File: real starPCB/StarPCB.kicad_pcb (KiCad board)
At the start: 2 copper layers, 19.6 x 19.2 mm, 5 parts, among them J1 +, J2 +, J4 -, J5 -

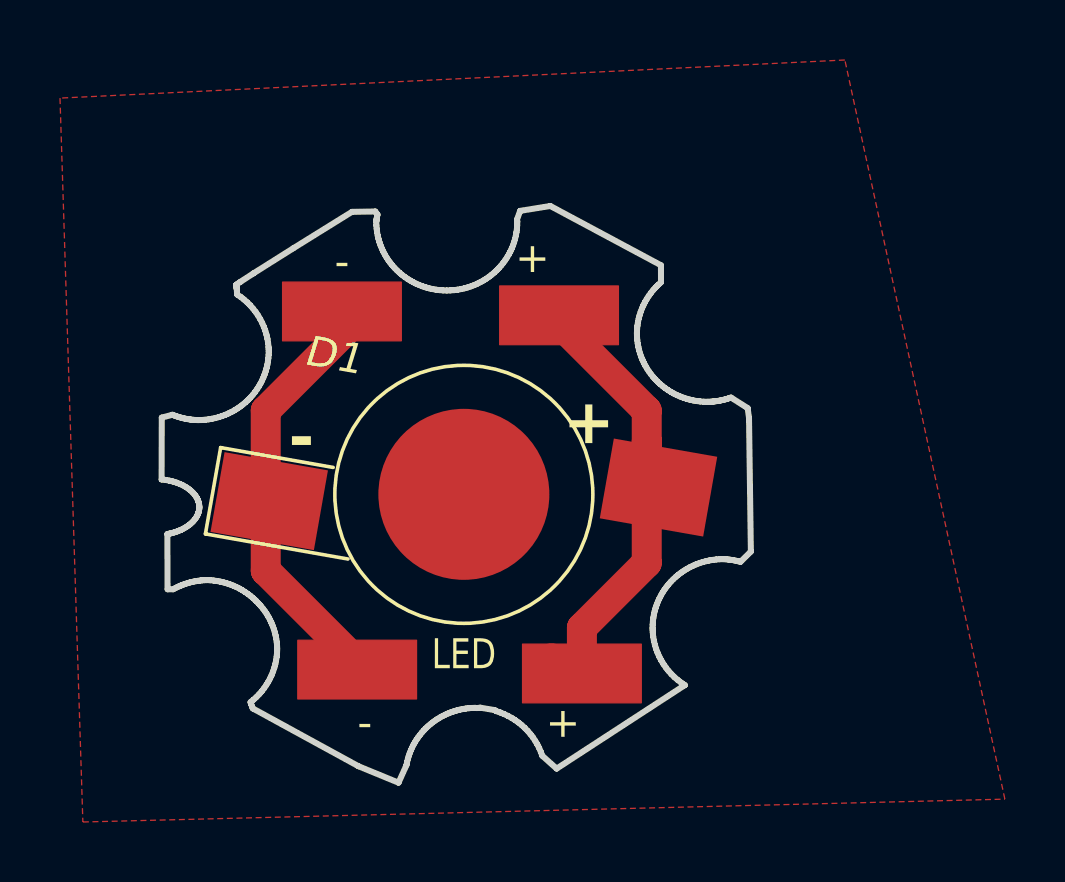
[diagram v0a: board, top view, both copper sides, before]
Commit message: new trace using shapes
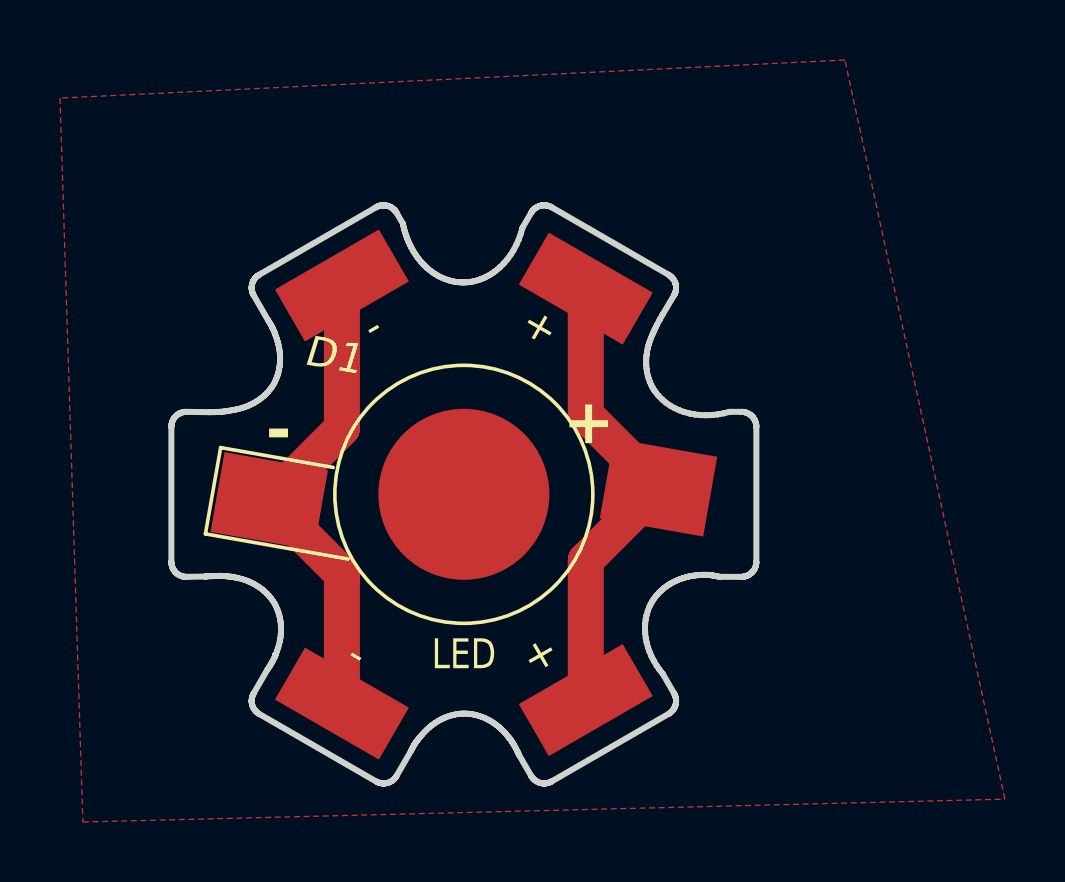
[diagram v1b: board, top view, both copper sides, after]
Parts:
- moved J1 2.13 mm to (123.5, 65.7), turned to -30 degrees
- moved J2 1.97 mm to (124.5, 81.4), turned to 30 degrees
- moved J5 0.77 mm to (116.4, 67.5), turned to 30 degrees
- moved J4 0.74 mm to (115.4, 79.5), turned to -30 degrees
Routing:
- net GND: track 14.7 -> 15.9 mm
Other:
- board size 19.6 x 19.2 mm -> 19.5 x 19.3 mm
